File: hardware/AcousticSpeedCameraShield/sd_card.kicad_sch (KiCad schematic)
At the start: 6 parts

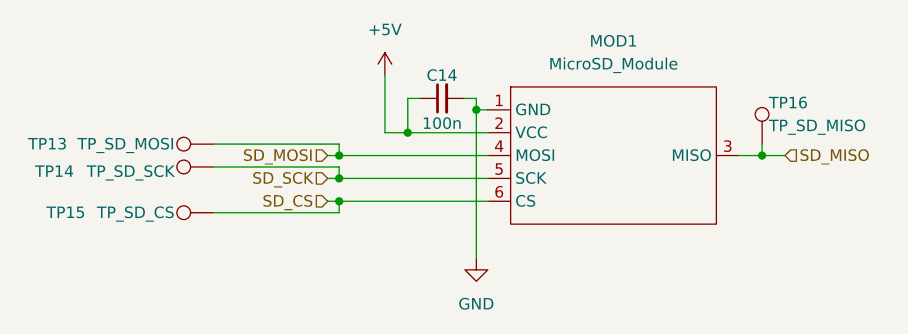
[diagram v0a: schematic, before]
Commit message: update MCU pin assignments
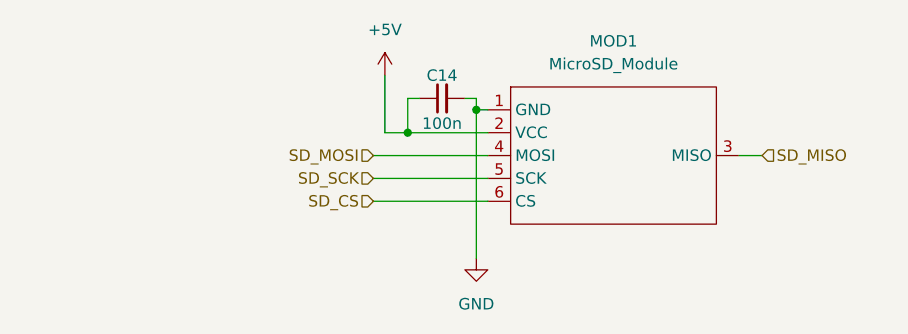
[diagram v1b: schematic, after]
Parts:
- removed TP13: TP_SD_MOSI, symbol Connector:TestPoint
- removed TP14: TP_SD_SCK, symbol Connector:TestPoint
- removed TP15: TP_SD_CS, symbol Connector:TestPoint
- removed TP16: TP_SD_MISO, symbol Connector:TestPoint
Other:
- title: (none) -> Interfejs Pamięci Masowej
